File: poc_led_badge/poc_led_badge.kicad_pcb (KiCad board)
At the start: 2 copper layers, 103.5 x 103.5 mm, 40 parts, among them SW1 SW_SPST

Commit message: update footprints
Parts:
- D1, D2, D3: footprint LED_SMD:LED_THT_SMD_Pads -> Project footprints:LED_THT_SMD_Pads
- SW1: footprint Button_Switch_SMD:SW_Tactile_SPST_KAN-28 -> Project footprints:SW_Tactile_SPST_KAN-28
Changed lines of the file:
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@@
 		(embedded_fonts no)
 	)
-	(footprint "LED_SMD:LED_THT_SMD_Pads"
+	(footprint "Project footprints:LED_THT_SMD_Pads"
 		(layer "F.Cu")
 		(at 130 85.125 -90)
@@
 			)
 		)
-		(property "Description" "Light emitting diode"
+		(property "Description" ""
 			(at 0 0 270)
 			(unlocked yes)
@@
 		(embedded_fonts no)
 	)
-	(footprint "LED_SMD:LED_THT_SMD_Pads"
+	(footprint "Project footprints:LED_THT_SMD_Pads"
 		(layer "F.Cu")
 		(at 86.625 47.75)
@@
 			)
 		)
-		(property "Description" "Light emitting diode"
+		(property "Description" ""
 			(at 0 0 0)
 			(unlocked yes)
@@
 		(embedded_fonts no)
 	)
-	(footprint "LED_SMD:LED_THT_SMD_Pads"
+	(footprint "Project footprints:LED_THT_SMD_Pads"
 		(layer "F.Cu")
 		(at 44.5 86 90)
@@
 			)
 		)
-		(property "Description" "Light emitting diode"
+		(property "Description" ""
 			(at 0 0 90)
 			(unlocked yes)
@@
 		(embedded_fonts no)
 	)
-	(footprint "Button_Switch_SMD:SW_Tactile_SPST_KAN-28"
+	(footprint "Project footprints:SW_Tactile_SPST_KAN-28"
 		(layer "F.Cu")
 		(at 49.411671 114.216889 130)
@@
 			)
 		)
-		(property "Datasheet" ""
-			(at -8.199999 -11.4 130)
+		(property "Datasheet" "https://www.chinadaier.com/wp-content/uploads/2017/12/PBS-02AKAN-28.pdf"
+			(at -8.2 -11.4 130)
 			(unlocked yes)
 			(layer "F.Fab")
@@
 			)
 		)
-		(property "Description" "Single Pole Single Throw (SPST) switch"
-			(at -8.199999 -11.4 130)
+		(property "Description" ""
+			(at -8.2 -11.4 130)
 			(unlocked yes)
 			(layer "F.Fab")
@@
 		(fp_line
 			(start 8.75 -5.75)
-			(end -8.749999 -5.75)
+			(end -8.75 -5.75)
 			(stroke
 				(width 0.1)
@@
 		)
 		(fp_line
-			(start 8.749999 -2.5)
+			(start 8.75 -2.5)
 			(end 8.75 -5.75)
 			(stroke
@@
 		(fp_line
 			(start 8.75 2.5)
-			(end 8.749999 5.75)
+			(end 8.75 5.75)
 			(stroke
 				(width 0.1)
@@
 		)
 		(fp_line
-			(start -8.749999 -5.75)
+			(start -8.75 -5.75)
 			(end -8.75 -2.5)
 			(stroke
@@
 		)
 		(fp_line
-			(start -8.749999 2.5)
+			(start -8.75 2.5)
 			(end -8.75 5.75)
 			(stroke
@@
 		(fp_line
 			(start -8.75 5.75)
-			(end 8.749999 5.75)
+			(end 8.75 5.75)
 			(stroke
 				(width 0.1)
@@
 		(fp_poly
 			(pts
-				(xy -1.35 -0.65) (xy 1.35 -0.650001) (xy 1.35 0.65) (xy -1.35 0.650001)
+				(xy -1.35 -0.65) (xy 1.35 -0.65) (xy 1.35 0.65) (xy -1.35 0.65)
 			)
 			(stroke
@@
 		(fp_line
 			(start 16.5 -2.75)
-			(end 16.5 2.750001)
+			(end 16.5 2.75)
 			(stroke
 				(width 0.05)
@@
 		)
 		(fp_line
-			(start 16.5 2.750001)
+			(start 16.5 2.75)
 			(end 9 2.75)
 			(stroke
@@
 		(fp_line
 			(start 9 2.75)
-			(end 9 6.000001)
+			(end 9 6)
 			(stroke
 				(width 0.05)
@@
 		)
 		(fp_line
-			(start 9 6.000001)
+			(start 9 6)
 			(end -9 6)
 			(stroke
@@
 		)
 		(fp_line
-			(start -9 -6.000001)
+			(start -9 -6)
 			(end 0 -6)
 			(stroke
@@
 		(fp_line
 			(start -9 -2.75)
-			(end -9 -6.000001)
+			(end -9 -6)
 			(stroke
 				(width 0.05)
@@
 		(fp_line
 			(start -9 -2.75)
-			(end -16.5 -2.750001)
+			(end -16.5 -2.75)
 			(stroke
 				(width 0.05)
@@
 		)
 		(fp_line
-			(start -16.5 -2.499999)
-			(end -16.5 -2.750001)
+			(start -16.499999 -2.5)
+			(end -16.5 -2.75)
 			(stroke
 				(width 0.05)
@@
 		(fp_line
 			(start -16.5 2.5)
-			(end -16.5 -2.499999)
+			(end -16.499999 -2.5)
 			(stroke
 				(width 0.05)
@@
 		)
 		(embedded_fonts no)
-		(model "${KICAD9_3DMODEL_DIR}/Button_Switch_SMD.3dshapes/SW_Tactile_SPST_NO_Straight_CK_PTS636Sx25SMTRLFS.wrl"
-			(offset
-				(xyz 0 0 0)
-			)
-			(scale
-				(xyz 1 1 1)
-			)
-			(rotate
-				(xyz 0 0 0)
-			)
-		)
 	)
 	(footprint ""
@@
 			"AAAAAAAAAAAAAAAAAAAAAAAAAAAAAAAAAAAAAAAAAAAAAAAAAAAAAAAAAAAAAAAAAAAAAAAAAAAA"
 			"AAAAAAAAAAAAAAAAAAAAAAAAAAAAAAAAAAAAAAAAAAAAAAAAAAAAAAAAAAAAAAAAAAAAAAAAAAAA"
-			"AAAAAAAAAAAAAAAAAAAAAAAAAAAAAAAAAAAAAAAAAAAAAAAAAAAAAAAAAAAAAAAAAAAAAAAA"
+			"AAAAAAAAAAAAAAAAAAAAAAAAAAAAAAAAAAAAAAAAAAAAAAAAAAAAAAAAAAAAAAAAAAAAAAAAAAAA"
+			"AAAAAAAAAAAAAAAAAAAAAAAAAAAAAAAAAAAAAAAAAAAAAAAAAAAAAAAAAAAAAAAAAAAAAAAAAAAA"
+			"AAAAAAAAAAAAAAAAAAAAAAAAAAAAAAAAAAAAAAAAAAAAAAAAAAAAAAAAAAAAAAAAAAAAAAAAAAAA"
+			"AAAAAAAAAAAAAAAAAAAAAAAAAAAAAAAAAAAAAAAAAAAAAAAAAAAAAAAAAAAAAAAAAAAAAAAAAAAA"
+			"AAAAAAAAAAAAAAAAAAAAAAAAAAAAAAAAAAAAAAAAAAAAAAAAAAAAAAAAAAAAAAAAAAAAAAAAAAAA"
+			"AAAAAAAAAAAAAAAAAAAAAAAAAAAAAAAAAAAAAAAAAAAAAAAAAAAAAAAAAAAAAAAAAAAAAAAAAAAA"
+			"AAAAAAAAAAAAAAAAAAAAAAAAAAAAAAAAAAAAAAAAAAAAAAAAAAAAAAAAAAAAAAAAAAAAAAAAAAAA"
+			"AAAAAAAAAAAAAAAAAAAAAAAAAAAAAAAAAAAAAAAAAAAAAAAAAAAAAAAAAAAAAAAAAAAAAAAAAAAA"
+			"AAAAAAAAAAAAAAAAAAAAAAAAAAAAAAAAAAAAAAAAAAAAAAAAAAAAAAAAAAAAAAAAAAAAAAAAAAAA"
+			"AAAAAAAAAAAAAAAAAAAAAAAAAAAAAAAAAAAAAAAAAAAAAAAAAAAAAAAAAAAAAAAAAAAAAAAAAAAA"
+			"AAAAAAAAAAAAAAAAAAAAAAAAAAAAAAAAAAAAAAAAAAAAAAAAAAAAAAAAAAAAAAAAAAAAAAAAAAAA"
+			"AAAAAAAAAAAAAAAAAAAAAAAAAAAAAAAAAAAAAAAAAAAAAAAAAAAAAAAAAAAAAAAAAAAAAAAAAAAA"
+			"AAAAAAAAAAAAAAAAAAAAAAAAAAAAAAAAAAAAAAAAAAAAAAAAAAAAAAAAAAAAAAAAAAAAAAAAAAAA"
+			"AAAAAAAAAAAAAAAAAAAAAAAAAAAAAAAAAAAAAAAAAAAAAAAAAAAAAAAAAAAAAAAAAAAAAAAAAAAA"
+			"AAAAAAAAAAAAAAAAAAAAAAAAAAAAAAAAAAAAAAAAAAAAAAAAAAAAAAAAAAAAAAAAAAAAAAAAAAAA"
+			"AAAAAAAAAAAAAAAAAAAAAAAAAAAAAAAAAAAAAAAAAAAAAAAAAAAAAAAAAAAAAAAAAAAAAAAAAAAA"
+			"AAAAAAAAAAAAAAAAAAAAAAAAAAAAAAAAAAAAAAAAAAAAAAAAAAAAAAAAAAAAAAAAAAAAAAAAAAAA"
+			"AAAAAAAAAAAAAAAAAAAAAAAAAAAAAAAAAAAAAAAAAAAAAAAAAAAAAAAAAAAAAAAAAAAAAAAAAAAA"
+			"AAAAAAAAAAAAAAAAAAAAAAAAAAAAAAAAAAAAAAAAAAAAAAAAAAAAAAAAAAAAAAAAAAAAAA=="
 		)
 	)

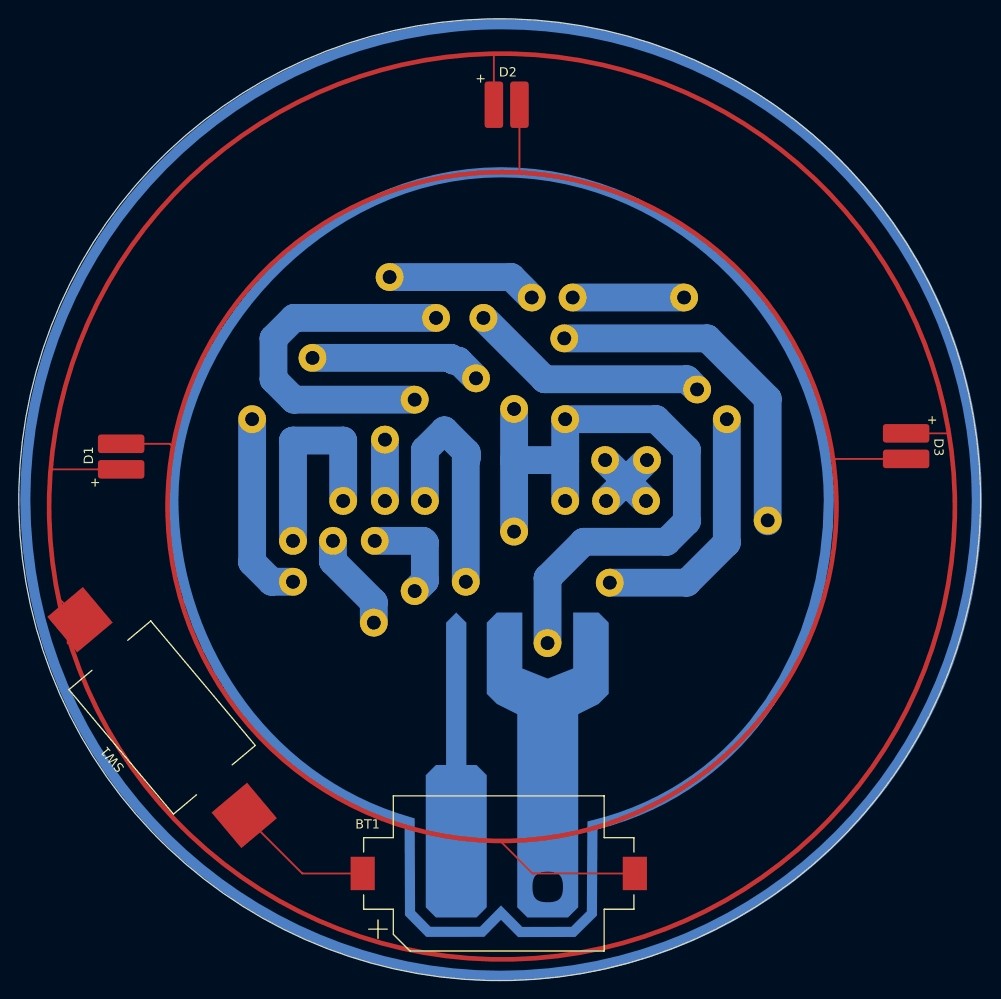
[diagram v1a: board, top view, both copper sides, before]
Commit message: thicker traces, more leds
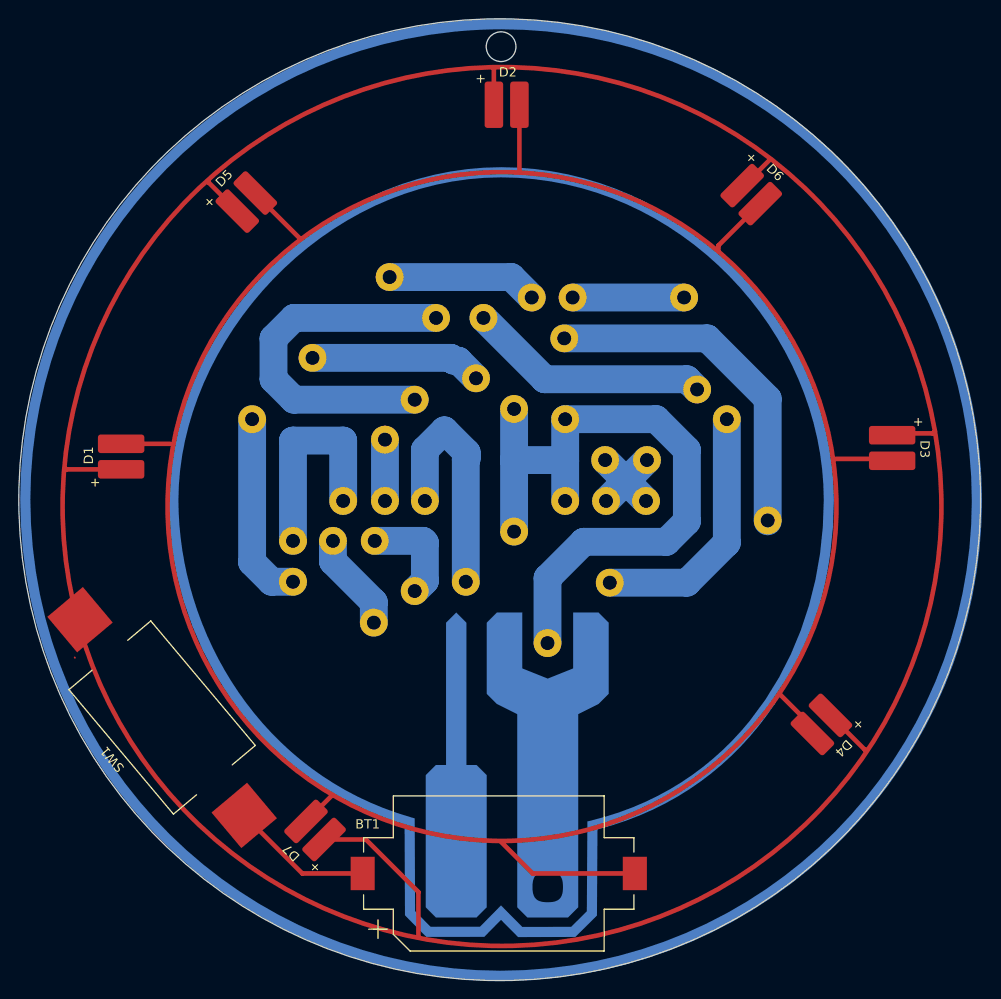
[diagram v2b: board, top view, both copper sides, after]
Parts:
- added D4: LED, Project footprints:LED_THT_SMD_Pads, F.Cu at (120.7, 115.4)
- added D5: LED, Project footprints:LED_THT_SMD_Pads, F.Cu at (58.2, 58.3)
- added D6: LED, Project footprints:LED_THT_SMD_Pads, F.Cu at (113.3, 57.7)
- added D7: LED, Project footprints:LED_THT_SMD_Pads, F.Cu at (65.4, 126.6)
- added REF**: MountingHole_3.2mm_M3_ISO7380, MountingHole:MountingHole_3.2mm_M3_ISO7380, F.Cu at (85.9, 42.0)
- moved D3 1.51 mm to (128.5, 85.3)
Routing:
- net Net-(D1-K): track 22.3 -> 50.9 mm
- net Net-(BT1--): track 40.1 -> 63.6 mm
